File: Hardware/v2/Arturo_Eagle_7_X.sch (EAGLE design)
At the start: 23 parts, among them T1 2SC1815, T3 2SC1815, T4 2SC1815, T5 2SC1815, T6 2SC1815, T7 2SC1815, T8 2SC1815, X1 22-23-2071

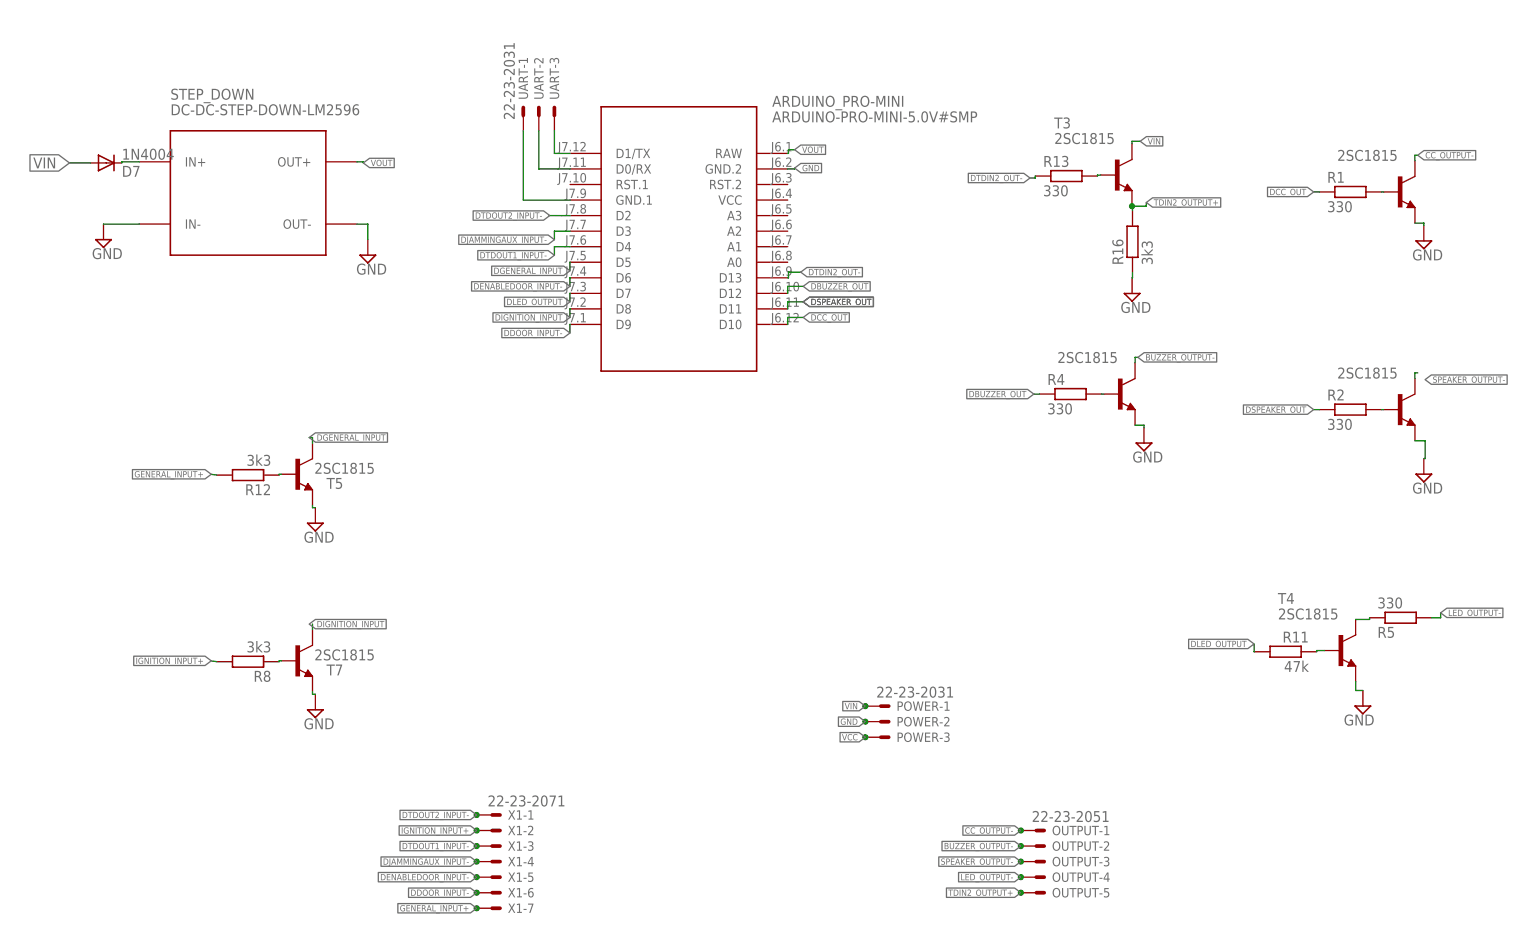
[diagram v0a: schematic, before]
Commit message: diseño de tomas
esta es la versión corregida que entregó tomas y es la que enviamos a fabricar
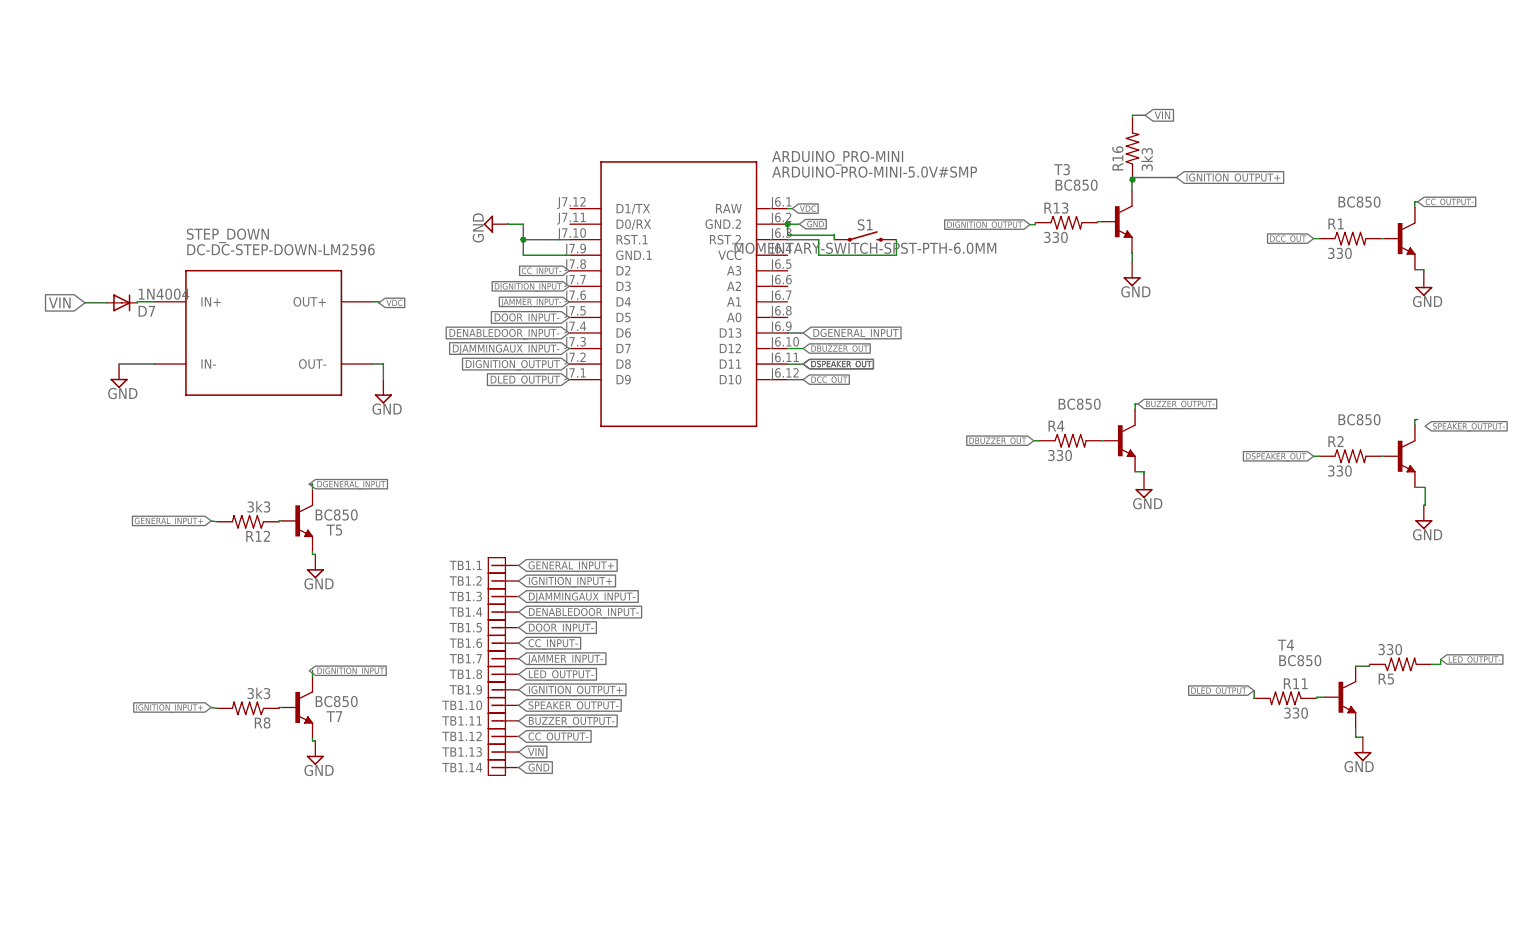
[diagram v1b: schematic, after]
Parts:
- removed OUTPUT: 22-23-2051, con-molex:22-23-2051
- removed POWER, UART: 22-23-2031, con-molex:22-23-2031
- removed X1: 22-23-2071, con-molex:22-23-2071
- added S1: MOMENTARY-SWITCH-SPST-PTH-6.0MM, SparkFun-Switches:MOMENTARY-SWITCH-SPST-PTH-6.0MM
- added TB1: (no value), libreria_PCB_Arturo:TB_PHOENIX
- R1, R12, R13, R16, R2, R4, R5, R8: device resistor:R-EU_0204/7 -> resistor:R-US_R0805
- R11: value 47k -> 330; device resistor:R-EU_0204/7 -> resistor:R-US_R0805
- T1, T3, T4, T5, T6, T7, T8: value 2SC1815 -> BC850; device transistor:2SC1815 -> transistor:BC850
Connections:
- net VOUT renamed VDC
- removed net DDOOR_INPUT-: ARDUINO_PRO-MINI.D9, X1-6.S
- removed net DTDIN2_OUT-: ARDUINO_PRO-MINI.D13, R13.1
- removed net DTDOUT1_INPUT-: ARDUINO_PRO-MINI.D4, X1-3.S
- removed net DTDOUT2_INPUT-: ARDUINO_PRO-MINI.D2, X1-1.S
- removed net N$7: ARDUINO_PRO-MINI.D1/TX, UART-3.S
- removed net N$8: ARDUINO_PRO-MINI.D0/RX, UART-2.S
- removed net N$9: ARDUINO_PRO-MINI.GND.1, UART-1.S
- removed net TDIN2_OUTPUT+: OUTPUT-5.S, R16.2, T3.E
- removed net VCC: POWER-3.S
- new net CC_INPUT-: ARDUINO_PRO-MINI.D2, TB1.6.1
- new net DIGNITION_OUTPUT: ARDUINO_PRO-MINI.D8, R13.1
- new net DOOR_INPUT-: ARDUINO_PRO-MINI.D5, TB1.5.1
- new net IGNITION_OUTPUT+: R16.1, T3.C, TB1.9.1
- new net JAMMER_INPUT-: ARDUINO_PRO-MINI.D4, TB1.7.1
- new net N$10: ARDUINO_PRO-MINI.RST.2, S1.2
- net BUZZER_OUTPUT-: now also TB1.11.1; no longer OUTPUT-2.S
- net CC_OUTPUT-: now also TB1.12.1; no longer OUTPUT-1.S
- net DENABLEDOOR_INPUT-: now also TB1.4.1; no longer X1-5.S
- net DGENERAL_INPUT: now also ARDUINO_PRO-MINI.D13; no longer ARDUINO_PRO-MINI.D5
- net DIGNITION_INPUT: now also ARDUINO_PRO-MINI.D3; no longer ARDUINO_PRO-MINI.D8
- net DJAMMINGAUX_INPUT-: now also ARDUINO_PRO-MINI.D7, TB1.3.1; no longer ARDUINO_PRO-MINI.D3, X1-4.S
- net DLED_OUTPUT: now also ARDUINO_PRO-MINI.D9; no longer ARDUINO_PRO-MINI.D7
- net GENERAL_INPUT+: now also TB1.1.1; no longer X1-7.S
- net GND: now also ARDUINO_PRO-MINI.GND.1, ARDUINO_PRO-MINI.RST.1, S1.1, T3.E, TB1.14.1; no longer POWER-2.S, R16.1
- net IGNITION_INPUT+: now also TB1.2.1; no longer X1-2.S
- net LED_OUTPUT-: now also TB1.8.1; no longer OUTPUT-4.S
- net SPEAKER_OUTPUT-: now also TB1.10.1; no longer OUTPUT-3.S
- net VIN: now also R16.2, TB1.13.1; no longer POWER-1.S, T3.C
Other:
- moved on the sheet: ARDUINO_PRO-MINI, D7, STEP_DOWN, T3, T4, T5, T7
